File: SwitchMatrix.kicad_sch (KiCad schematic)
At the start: 134 parts, among them K1 Home, K10 I, K11 O, K12 P, K13 Back Space, K14 Delete, K15 1, K16 2, K17 Shift, K18 End, K19 Esc, K2 Tab, K20 A, K21 S, K22 D, K23 F, K24 G, K25 H, K26 J, K27 K, K28 L, K29 ;, K3 Q, K30 ', K31 Return, K32 4, K33 5, K34 Super, K35 Vol +, K36 Shift, K37 Z, K38 X, K39 C, K4 W, K40 V, K41 B, K42 N, K43 M, K44 ,, K45 ., K46 /, K47 Shift, K48 7, K49 8, K5 E, K50 9, K51 N, K52 Vol -, K53 Ctrl, K54 Alt, K55 Super, K56 &dArr;, K57 Blank, K58 &uArr;, K59 Alt, K6 R, K60 0, K61 Enter, K62 Fn, K63 &larr;, K64 &darr;, K7 T, K8 Y, K9 U

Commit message: test prod files for jlc quote, wrong diode footprint 🤦‍
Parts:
- D1, D10, D11, D12, D13, D14, D15, D16, D18, D19, D2, D20, D21, D22, D23, D24, D25, D26, D27, D28, D29, D3, D30, D31, D32, D33, D35, D36, D37, D38, D39, D4, D40, D41, D42, D43, D44, D45, D46, D47, D48, D49, D5, D50, D52, D53, D54, D55, D56, D57, D58, D59, D6, D60, D61, D62, D63, D64, D7, D8, D9: value D -> 1N4148W
- K22: value D -> 1N4148W; footprint PCM_Switch_Keyboard_Hotswap_Kailh:SW_Hotswap_Kailh_MX_1.00u -> Diode_SMD:D_0805_2012Metric_Pad1.15x1.40mm_HandSolder
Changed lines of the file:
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@@
 			)
 		)
-		(property "Value" "D"
+		(property "Value" "1N4148W"
 			(at 39.37 160.02 90)
 			(effects
@@
 			)
 		)
-		(property "Value" "D"
+		(property "Value" "1N4148W"
 			(at 373.38 134.62 90)
 			(effects
@@
 			)
 		)
-		(property "Value" "D"
+		(property "Value" "1N4148W"
 			(at 119.38 139.7 0)
 			(effects
@@
 			)
 		)
-		(property "Footprint" "PCM_Switch_Keyboard_Hotswap_Kailh:SW_Hotswap_Kailh_MX_1.00u"
+		(property "Footprint" "Diode_SMD:D_0805_2012Metric_Pad1.15x1.40mm_HandSolder"
 			(at 119.38 137.16 0)
 			(effects
@@
 			)
 		)
-		(property "Value" "D"
+		(property "Value" "1N4148W"
 			(at 373.38 172.72 90)
 			(effects
@@
 			)
 		)
-		(property "Value" "D"
+		(property "Value" "1N4148W"
 			(at 234.95 172.72 90)
 			(effects
@@
 			)
 		)
-		(property "Value" "D"
+		(property "Value" "1N4148W"
 			(at 105.41 160.02 90)
 			(effects
@@
 			)
 		)
-		(property "Value" "D"
+		(property "Value" "1N4148W"
 			(at 304.8 166.37 90)
 			(effects
@@
 			)
 		)
-		(property "Value" "D"
+		(property "Value" "1N4148W"
 			(at 64.77 160.02 90)
 			(effects
@@
 			)
 		)
-		(property "Value" "D"
+		(property "Value" "1N4148W"
 			(at 105.41 147.32 90)
 			(effects
@@
 			)
 		)
-		(property "Value" "D"
+		(property "Value" "1N4148W"
 			(at 227.33 160.02 90)
 			(effects
@@
 			)
 		)
-		(property "Value" "D"
+		(property "Value" "1N4148W"
 			(at 207.01 160.02 90)
 			(effects
@@
 			)
 		)
-		(property "Value" "D"
+		(property "Value" "1N4148W"
 			(at 353.06 147.32 90)
 			(effects
@@
 			)
 		)
-		(property "Value" "D"
+		(property "Value" "1N4148W"
 			(at 125.73 147.32 90)
 			(effects
@@
 			)
 		)
-		(property "Value" "D"
+		(property "Value" "1N4148W"
 			(at 247.65 134.62 90)
 			(effects
@@
 			)
 		)
-		(property "Value" "D"
+		(property "Value" "1N4148W"
 			(at 64.77 134.62 90)
 			(effects
@@
 			)
 		)
-		(property "Value" "D"
+		(property "Value" "1N4148W"
 			(at 146.05 134.62 90)
 			(effects
@@
 			)
 		)
-		(property "Value" "D"
+		(property "Value" "1N4148W"
 			(at 85.09 147.32 90)
 			(effects
@@
 			)
 		)
-		(property "Value" "D"
+		(property "Value" "1N4148W"
 			(at 207.01 147.32 90)
 			(effects
@@
 			)
 		)
-		(property "Value" "D"
+		(property "Value" "1N4148W"
 			(at 39.37 147.32 90)
 			(effects
@@
 			)
 		)
-		(property "Value" "D"
+		(property "Value" "1N4148W"
 			(at 247.65 147.32 90)
 			(effects
@@
 			)
 		)
-		(property "Value" "D"
+		(property "Value" "1N4148W"
 			(at 125.73 134.62 90)
 			(effects
@@
 			)
 		)
-		(property "Value" "D"
+		(property "Value" "1N4148W"
 			(at 85.09 160.02 90)
 			(effects
@@
 			)
 		)
-		(property "Value" "D"
+		(property "Value" "1N4148W"
 			(at 288.29 134.62 90)
 			(effects
@@
 			)
 		)
-		(property "Value" "D"
+		(property "Value" "1N4148W"
 			(at 67.31 172.72 90)
 			(effects
@@
 			)
 		)
-		(property "Value" "D"
+		(property "Value" "1N4148W"
 			(at 186.69 134.62 90)
 			(effects
@@
 			)
 		)
-		(property "Value" "D"
+		(property "Value" "1N4148W"
 			(at 176.53 172.72 90)
 			(effects
@@
 			)
 		)
-		(property "Value" "D"
+		(property "Value" "1N4148W"
 			(at 118.11 172.72 90)
 			(effects
@@
 			)
 		)
-		(property "Value" "D"
+		(property "Value" "1N4148W"
 			(at 166.37 160.02 90)
 			(effects
@@
 			)
 		)
-		(property "Value" "D"
+		(property "Value" "1N4148W"
 			(at 227.33 147.32 90)
 			(effects
@@
 			)
 		)
-		(property "Value" "D"
+		(property "Value" "1N4148W"
 			(at 92.71 172.72 90)
 			(effects
@@
 			)
 		)
-		(property "Value" "D"
+		(property "Value" "1N4148W"
 			(at 373.38 160.02 90)
 			(effects
@@
 			)
 		)
-		(property "Value" "D"
+		(property "Value" "1N4148W"
 			(at 105.41 134.62 90)
 			(effects
@@
 			)
 		)
-		(property "Value" "D"
+		(property "Value" "1N4148W"
 			(at 353.06 160.02 90)
 			(effects
@@
 			)
 		)
-		(property "Value" "D"
+		(property "Value" "1N4148W"
 			(at 146.05 147.32 90)
 			(effects
@@
 			)
 		)
-		(property "Value" "D"
+		(property "Value" "1N4148W"
 			(at 166.37 134.62 90)
 			(effects
@@
 			)
 		)
-		(property "Value" "D"
+		(property "Value" "1N4148W"
 			(at 209.55 172.72 90)
 			(effects
@@
 			)
 		)
-		(property "Value" "D"
+		(property "Value" "1N4148W"
 			(at 247.65 160.02 90)
 			(effects
@@
 			)
 		)
-		(property "Value" "D"
+		(property "Value" "1N4148W"
 			(at 267.97 147.32 90)
 			(effects
@@
 			)
 		)
-		(property "Value" "D"
+		(property "Value" "1N4148W"
 			(at 331.47 134.62 90)
 			(effects
@@
 			)
 		)
-		(property "Value" "D"
+		(property "Value" "1N4148W"
 			(at 207.01 134.62 90)
 			(effects
@@
 			)
 		)
-		(property "Value" "D"
+		(property "Value" "1N4148W"
 			(at 288.29 147.32 90)
 			(effects
@@
 			)
 		)
-		(property "Value" "D"
+		(property "Value" "1N4148W"
 			(at 39.37 134.62 90)
 			(effects
@@
 			)
 		)
-		(property "Value" "D"
+		(property "Value" "1N4148W"
 			(at 284.48 179.07 90)
 			(effects
@@
 			)
 		)
-		(property "Value" "D"
+		(property "Value" "1N4148W"
 			(at 267.97 134.62 90)
 			(effects
@@
 			)
 		)
-		(property "Value" "D"
+		(property "Value" "1N4148W"
 			(at 304.8 179.07 90)
 			(effects
@@
 			)
 		)
-		(property "Value" "D"
+		(property "Value" "1N4148W"
 			(at 64.77 147.32 90)
 			(effects
@@
 			)
 		)
-		(property "Value" "D"
+		(property "Value" "1N4148W"
 			(at 227.33 134.62 90)
 			(effects
@@
 			)
 		)
-		(property "Value" "D"
+		(property "Value" "1N4148W"
 			(at 353.06 134.62 90)
 			(effects
@@
 			)
 		)
-		(property "Value" "D"
+		(property "Value" "1N4148W"
 			(at 331.47 147.32 90)
 			(effects
@@
 			)
 		)
-		(property "Value" "D"
+		(property "Value" "1N4148W"
 			(at 331.47 160.02 90)
 			(effects
@@
 			)
 		)
-		(property "Value" "D"
+		(property "Value" "1N4148W"
 			(at 39.37 172.72 90)
 			(effects
@@
 			)
 		)
-		(property "Value" "D"
+		(property "Value" "1N4148W"
 			(at 146.05 160.02 90)
 			(effects
@@
 			)
 		)
-		(property "Value" "D"
+		(property "Value" "1N4148W"
 			(at 186.69 160.02 90)
 			(effects
@@
 			)
 		)
-		(property "Value" "D"
+		(property "Value" "1N4148W"
 			(at 373.38 147.32 90)
 			(effects
@@
 			)
 		)
-		(property "Value" "D"
+		(property "Value" "1N4148W"
 			(at 125.73 160.02 90)
 			(effects
@@
 			)
 		)
-		(property "Value" "D"
+		(property "Value" "1N4148W"
 			(at 267.97 160.02 90)
 			(effects
@@
 			)
 		)
-		(property "Value" "D"
+		(property "Value" "1N4148W"
 			(at 353.06 172.72 90)
 			(effects
@@
 			)
 		)
-		(property "Value" "D"
+		(property "Value" "1N4148W"
 			(at 143.51 172.72 90)
 			(effects
@@
 			)
 		)
-		(property "Value" "D"
+		(property "Value" "1N4148W"
 			(at 85.09 134.62 90)
 			(effects
@@
 			)
 		)
-		(property "Value" "D"
+		(property "Value" "1N4148W"
 			(at 186.69 147.32 90)
 			(effects
@@
 			)
 		)
-		(property "Value" "D"
+		(property "Value" "1N4148W"
 			(at 166.37 147.32 90)
 			(effects
@@
 			)
 		)
-		(property "Value" "D"
+		(property "Value" "1N4148W"
 			(at 325.12 179.07 90)
 			(effects

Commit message: sod-128 diodes, still wrong it was supposed to be 123
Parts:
- D1, D10, D11, D12, D13, D14, D15, D16, D18, D19, D2, D20, D21, D22, D23, D24, D25, D26, D27, D28, D29, D3, D30, D31, D32, D33, D35, D36, D37, D38, D39, D4, D40, D41, D42, D43, D44, D45, D46, D47, D48, D49, D5, D50, D52, D53, D54, D55, D56, D57, D58, D59, D6, D60, D61, D62, D63, D64, D7, D8, D9: footprint Diode_SMD:D_0805_2012Metric_Pad1.15x1.40mm_HandSolder -> Diode_SMD:D_SOD-123
- K22: footprint Diode_SMD:D_0805_2012Metric_Pad1.15x1.40mm_HandSolder -> PCM_Switch_Keyboard_Hotswap_Kailh:SW_Hotswap_Kailh_MX_1.00u

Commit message: last before prod
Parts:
- K22: value 1N4148W -> D
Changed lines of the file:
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@@
 			)
 		)
-		(property "Value" "1N4148W"
+		(property "Value" "D"
 			(at 119.38 139.7 0)
 			(effects

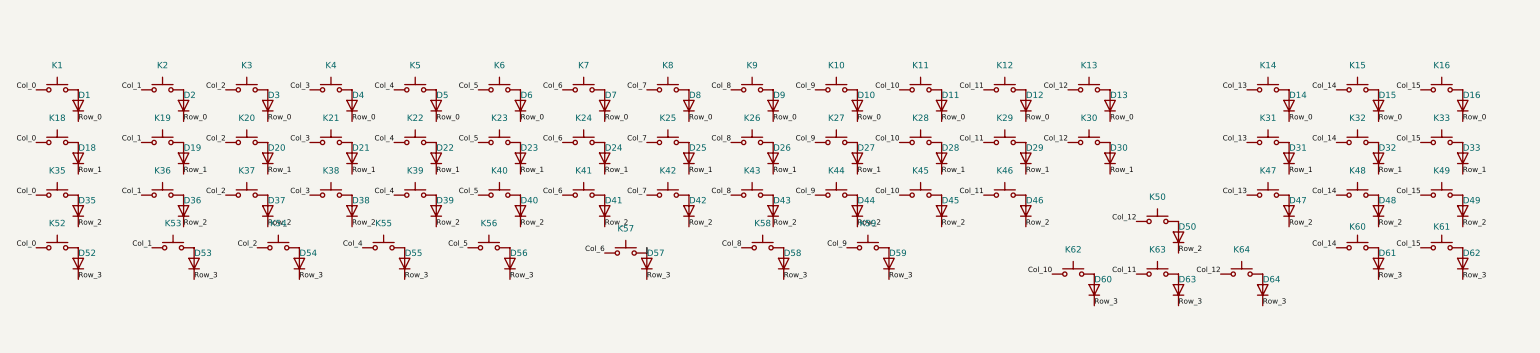
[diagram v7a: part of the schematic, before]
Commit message: add part nums for bom
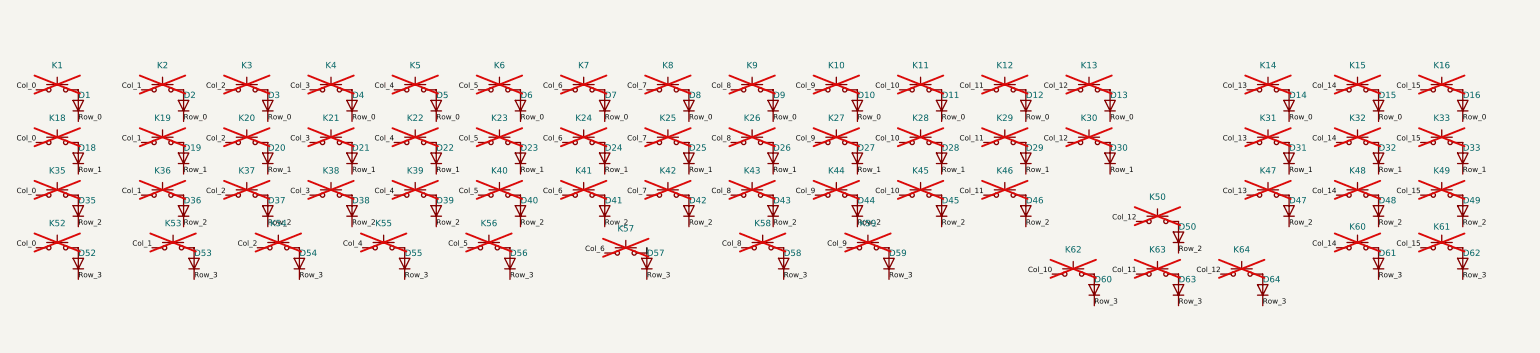
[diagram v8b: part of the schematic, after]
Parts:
- D1, D10, D11, D12, D13, D14, D15, D16, D18, D19, D2, D20, D21, D22, D23, D24, D25, D26, D27, D28, D29, D3, D30, D31, D32, D33, D35, D36, D37, D38, D39, D4, D40, D41, D42, D43, D44, D45, D46, D47, D48, D49, D5, D50, D52, D53, D54, D55, D56, D57, D58, D59, D6, D60, D61, D62, D63, D64, D7, D8, D9: LCSC (none) -> C2828417; Manufacturer (none) -> 1N4148W; Type (none) -> SMD
- D17, D34, D51: Type (none) -> DNS
- JP10, JP2, JP3, JP4, JP5, JP9: now left out of the parts list
- K1: value Home -> Kailh Hotswap Socket; Comment (none) -> Do Not Substitute; Digikey (none) -> 1528-4958-ND; MPN (none) -> 4958; Manufacturer (none) -> Adafruit; Type (none) -> SMD; now not fitted
- K10: value I -> Kailh Hotswap Socket; Comment (none) -> Do Not Substitute; Digikey (none) -> 1528-4958-ND; MPN (none) -> 4958; Manufacturer (none) -> Adafruit; Type (none) -> SMD; now not fitted
- K11: value O -> Kailh Hotswap Socket; Comment (none) -> Do Not Substitute; Digikey (none) -> 1528-4958-ND; MPN (none) -> 4958; Manufacturer (none) -> Adafruit; Type (none) -> SMD; now not fitted
- K12: value P -> Kailh Hotswap Socket; Comment (none) -> Do Not Substitute; Digikey (none) -> 1528-4958-ND; MPN (none) -> 4958; Manufacturer (none) -> Adafruit; Type (none) -> SMD; now not fitted
- K13: value Back Space -> Kailh Hotswap Socket; Comment (none) -> Do Not Substitute; Digikey (none) -> 1528-4958-ND; MPN (none) -> 4958; Manufacturer (none) -> Adafruit; Type (none) -> SMD; now not fitted
- K14: value Delete -> Kailh Hotswap Socket; Comment (none) -> Do Not Substitute; Digikey (none) -> 1528-4958-ND; MPN (none) -> 4958; Manufacturer (none) -> Adafruit; Type (none) -> SMD; now not fitted
- K15: value 1 -> Kailh Hotswap Socket; Comment (none) -> Do Not Substitute; Digikey (none) -> 1528-4958-ND; MPN (none) -> 4958; Manufacturer (none) -> Adafruit; Type (none) -> SMD; now not fitted
- K16: value 2 -> Kailh Hotswap Socket; Comment (none) -> Do Not Substitute; Digikey (none) -> 1528-4958-ND; MPN (none) -> 4958; Manufacturer (none) -> Adafruit; Type (none) -> SMD; now not fitted
- K17: value Shift -> Kailh Hotswap Socket; Comment (none) -> Do Not Substitute; Digikey (none) -> 1528-4958-ND; MPN (none) -> 4958; Manufacturer (none) -> Adafruit; Type (none) -> SMD
- K18: value End -> Kailh Hotswap Socket; Comment (none) -> Do Not Substitute; Digikey (none) -> 1528-4958-ND; MPN (none) -> 4958; Manufacturer (none) -> Adafruit; Type (none) -> SMD; now not fitted
- K19: value Esc -> Kailh Hotswap Socket; Comment (none) -> Do Not Substitute; Digikey (none) -> 1528-4958-ND; MPN (none) -> 4958; Manufacturer (none) -> Adafruit; Type (none) -> SMD; now not fitted
- K2: value Tab -> Kailh Hotswap Socket; Comment (none) -> Do Not Substitute; Digikey (none) -> 1528-4958-ND; MPN (none) -> 4958; Manufacturer (none) -> Adafruit; Type (none) -> SMD; now not fitted
- K20: value A -> Kailh Hotswap Socket; Comment (none) -> Do Not Substitute; Digikey (none) -> 1528-4958-ND; MPN (none) -> 4958; Manufacturer (none) -> Adafruit; Type (none) -> SMD; now not fitted
- K21: value S -> Kailh Hotswap Socket; Comment (none) -> Do Not Substitute; Digikey (none) -> 1528-4958-ND; MPN (none) -> 4958; Manufacturer (none) -> Adafruit; Type (none) -> SMD; now not fitted
- K22: value D -> Kailh Hotswap Socket; Comment (none) -> Do Not Substitute; Digikey (none) -> 1528-4958-ND; MPN (none) -> 4958; Manufacturer (none) -> Adafruit; Type (none) -> SMD; now not fitted
- K23: value F -> Kailh Hotswap Socket; Comment (none) -> Do Not Substitute; Digikey (none) -> 1528-4958-ND; MPN (none) -> 4958; Manufacturer (none) -> Adafruit; Type (none) -> SMD; now not fitted
- K24: value G -> Kailh Hotswap Socket; Comment (none) -> Do Not Substitute; Digikey (none) -> 1528-4958-ND; MPN (none) -> 4958; Manufacturer (none) -> Adafruit; Type (none) -> SMD; now not fitted
- K25: value H -> Kailh Hotswap Socket; Comment (none) -> Do Not Substitute; Digikey (none) -> 1528-4958-ND; MPN (none) -> 4958; Manufacturer (none) -> Adafruit; Type (none) -> SMD; now not fitted
- K26: value J -> Kailh Hotswap Socket; Comment (none) -> Do Not Substitute; Digikey (none) -> 1528-4958-ND; MPN (none) -> 4958; Manufacturer (none) -> Adafruit; Type (none) -> SMD; now not fitted
- K27: value K -> Kailh Hotswap Socket; Comment (none) -> Do Not Substitute; Digikey (none) -> 1528-4958-ND; MPN (none) -> 4958; Manufacturer (none) -> Adafruit; Type (none) -> SMD; now not fitted
- K28: value L -> Kailh Hotswap Socket; Comment (none) -> Do Not Substitute; Digikey (none) -> 1528-4958-ND; MPN (none) -> 4958; Manufacturer (none) -> Adafruit; Type (none) -> SMD; now not fitted
- K29: value ; -> Kailh Hotswap Socket; Comment (none) -> Do Not Substitute; Digikey (none) -> 1528-4958-ND; MPN (none) -> 4958; Manufacturer (none) -> Adafruit; Type (none) -> SMD; now not fitted
- K3: value Q -> Kailh Hotswap Socket; Comment (none) -> Do Not Substitute; Digikey (none) -> 1528-4958-ND; MPN (none) -> 4958; Manufacturer (none) -> Adafruit; Type (none) -> SMD; now not fitted
- K30: value ' -> Kailh Hotswap Socket; Comment (none) -> Do Not Substitute; Digikey (none) -> 1528-4958-ND; MPN (none) -> 4958; Manufacturer (none) -> Adafruit; Type (none) -> SMD; now not fitted
- K31: value Return -> Kailh Hotswap Socket; Comment (none) -> Do Not Substitute; Digikey (none) -> 1528-4958-ND; MPN (none) -> 4958; Manufacturer (none) -> Adafruit; Type (none) -> SMD; now not fitted
- K32: value 4 -> Kailh Hotswap Socket; Comment (none) -> Do Not Substitute; Digikey (none) -> 1528-4958-ND; MPN (none) -> 4958; Manufacturer (none) -> Adafruit; Type (none) -> SMD; now not fitted
- K33: value 5 -> Kailh Hotswap Socket; Comment (none) -> Do Not Substitute; Digikey (none) -> 1528-4958-ND; MPN (none) -> 4958; Manufacturer (none) -> Adafruit; Type (none) -> SMD; now not fitted
- K34: value Super -> Kailh Hotswap Socket; Comment (none) -> Do Not Substitute; Digikey (none) -> 1528-4958-ND; MPN (none) -> 4958; Manufacturer (none) -> Adafruit; Type (none) -> SMD
- K35: value Vol + -> Kailh Hotswap Socket; Comment (none) -> Do Not Substitute; Digikey (none) -> 1528-4958-ND; MPN (none) -> 4958; Manufacturer (none) -> Adafruit; Type (none) -> SMD; now not fitted
- K36, K47: value Shift -> Kailh Hotswap Socket; Comment (none) -> Do Not Substitute; Digikey (none) -> 1528-4958-ND; MPN (none) -> 4958; Manufacturer (none) -> Adafruit; Type (none) -> SMD; now not fitted
- K37: value Z -> Kailh Hotswap Socket; Comment (none) -> Do Not Substitute; Digikey (none) -> 1528-4958-ND; MPN (none) -> 4958; Manufacturer (none) -> Adafruit; Type (none) -> SMD; now not fitted
- K38: value X -> Kailh Hotswap Socket; Comment (none) -> Do Not Substitute; Digikey (none) -> 1528-4958-ND; MPN (none) -> 4958; Manufacturer (none) -> Adafruit; Type (none) -> SMD; now not fitted
- K39: value C -> Kailh Hotswap Socket; Comment (none) -> Do Not Substitute; Digikey (none) -> 1528-4958-ND; MPN (none) -> 4958; Manufacturer (none) -> Adafruit; Type (none) -> SMD; now not fitted
- K4: value W -> Kailh Hotswap Socket; Comment (none) -> Do Not Substitute; Digikey (none) -> 1528-4958-ND; MPN (none) -> 4958; Manufacturer (none) -> Adafruit; Type (none) -> SMD; now not fitted
- K40: value V -> Kailh Hotswap Socket; Comment (none) -> Do Not Substitute; Digikey (none) -> 1528-4958-ND; MPN (none) -> 4958; Manufacturer (none) -> Adafruit; Type (none) -> SMD; now not fitted
- K41: value B -> Kailh Hotswap Socket; Comment (none) -> Do Not Substitute; Digikey (none) -> 1528-4958-ND; MPN (none) -> 4958; Manufacturer (none) -> Adafruit; Type (none) -> SMD; now not fitted
- K42: value N -> Kailh Hotswap Socket; Comment (none) -> Do Not Substitute; Digikey (none) -> 1528-4958-ND; MPN (none) -> 4958; Manufacturer (none) -> Adafruit; Type (none) -> SMD; now not fitted
- K43: value M -> Kailh Hotswap Socket; Comment (none) -> Do Not Substitute; Digikey (none) -> 1528-4958-ND; MPN (none) -> 4958; Manufacturer (none) -> Adafruit; Type (none) -> SMD; now not fitted
- K44: value , -> Kailh Hotswap Socket; Comment (none) -> Do Not Substitute; Digikey (none) -> 1528-4958-ND; MPN (none) -> 4958; Manufacturer (none) -> Adafruit; Type (none) -> SMD; now not fitted
- K45: value . -> Kailh Hotswap Socket; Comment (none) -> Do Not Substitute; Digikey (none) -> 1528-4958-ND; MPN (none) -> 4958; Manufacturer (none) -> Adafruit; Type (none) -> SMD; now not fitted
- K46: value / -> Kailh Hotswap Socket; Comment (none) -> Do Not Substitute; Digikey (none) -> 1528-4958-ND; MPN (none) -> 4958; Manufacturer (none) -> Adafruit; Type (none) -> SMD; now not fitted
- K48: value 7 -> Kailh Hotswap Socket; Comment (none) -> Do Not Substitute; Digikey (none) -> 1528-4958-ND; MPN (none) -> 4958; Manufacturer (none) -> Adafruit; Type (none) -> SMD; now not fitted
- K49: value 8 -> Kailh Hotswap Socket; Comment (none) -> Do Not Substitute; Digikey (none) -> 1528-4958-ND; MPN (none) -> 4958; Manufacturer (none) -> Adafruit; Type (none) -> SMD; now not fitted
- K5: value E -> Kailh Hotswap Socket; Comment (none) -> Do Not Substitute; Digikey (none) -> 1528-4958-ND; MPN (none) -> 4958; Manufacturer (none) -> Adafruit; Type (none) -> SMD; now not fitted
- K50: value 9 -> Kailh Hotswap Socket; Comment (none) -> Do Not Substitute; Digikey (none) -> 1528-4958-ND; MPN (none) -> 4958; Manufacturer (none) -> Adafruit; Type (none) -> SMD; now not fitted
- K51: value N -> Kailh Hotswap Socket; Comment (none) -> Do Not Substitute; Digikey (none) -> 1528-4958-ND; MPN (none) -> 4958; Manufacturer (none) -> Adafruit; Type (none) -> SMD
- K52: value Vol - -> Kailh Hotswap Socket; Comment (none) -> Do Not Substitute; Digikey (none) -> 1528-4958-ND; MPN (none) -> 4958; Manufacturer (none) -> Adafruit; Type (none) -> SMD; now not fitted
- K53: value Ctrl -> Kailh Hotswap Socket; Comment (none) -> Do Not Substitute; Digikey (none) -> 1528-4958-ND; MPN (none) -> 4958; Manufacturer (none) -> Adafruit; Type (none) -> SMD; now not fitted
- K54, K59: value Alt -> Kailh Hotswap Socket; Comment (none) -> Do Not Substitute; Digikey (none) -> 1528-4958-ND; MPN (none) -> 4958; Manufacturer (none) -> Adafruit; Type (none) -> SMD; now not fitted
- K55: value Super -> Kailh Hotswap Socket; Comment (none) -> Do Not Substitute; Digikey (none) -> 1528-4958-ND; MPN (none) -> 4958; Manufacturer (none) -> Adafruit; Type (none) -> SMD; now not fitted
- K56: value &dArr; -> Kailh Hotswap Socket; Comment (none) -> Do Not Substitute; Digikey (none) -> 1528-4958-ND; MPN (none) -> 4958; Manufacturer (none) -> Adafruit; Type (none) -> SMD; now not fitted
- K57: value Blank -> Kailh Hotswap Socket; Comment (none) -> Do Not Substitute; Digikey (none) -> 1528-4958-ND; MPN (none) -> 4958; Manufacturer (none) -> Adafruit; Type (none) -> SMD; now not fitted
- K58: value &uArr; -> Kailh Hotswap Socket; Comment (none) -> Do Not Substitute; Digikey (none) -> 1528-4958-ND; MPN (none) -> 4958; Manufacturer (none) -> Adafruit; Type (none) -> SMD; now not fitted
- K6: value R -> Kailh Hotswap Socket; Comment (none) -> Do Not Substitute; Digikey (none) -> 1528-4958-ND; MPN (none) -> 4958; Manufacturer (none) -> Adafruit; Type (none) -> SMD; now not fitted
- K60: value 0 -> Kailh Hotswap Socket; Comment (none) -> Do Not Substitute; Digikey (none) -> 1528-4958-ND; MPN (none) -> 4958; Manufacturer (none) -> Adafruit; Type (none) -> SMD; now not fitted
- K61: value Enter -> Kailh Hotswap Socket; Comment (none) -> Do Not Substitute; Digikey (none) -> 1528-4958-ND; MPN (none) -> 4958; Manufacturer (none) -> Adafruit; Type (none) -> SMD; now not fitted
- K62: value Fn -> Kailh Hotswap Socket; Comment (none) -> Do Not Substitute; Digikey (none) -> 1528-4958-ND; MPN (none) -> 4958; Manufacturer (none) -> Adafruit; Type (none) -> SMD; now not fitted
- K63: value &larr; -> Kailh Hotswap Socket; Comment (none) -> Do Not Substitute; Digikey (none) -> 1528-4958-ND; MPN (none) -> 4958; Manufacturer (none) -> Adafruit; Type (none) -> SMD; now not fitted
- K64: value &darr; -> Kailh Hotswap Socket; Comment (none) -> Do Not Substitute; Digikey (none) -> 1528-4958-ND; MPN (none) -> 4958; Manufacturer (none) -> Adafruit; Type (none) -> SMD; now not fitted
- K7: value T -> Kailh Hotswap Socket; Comment (none) -> Do Not Substitute; Digikey (none) -> 1528-4958-ND; MPN (none) -> 4958; Manufacturer (none) -> Adafruit; Type (none) -> SMD; now not fitted
- K8: value Y -> Kailh Hotswap Socket; Comment (none) -> Do Not Substitute; Digikey (none) -> 1528-4958-ND; MPN (none) -> 4958; Manufacturer (none) -> Adafruit; Type (none) -> SMD; now not fitted
- K9: value U -> Kailh Hotswap Socket; Comment (none) -> Do Not Substitute; Digikey (none) -> 1528-4958-ND; MPN (none) -> 4958; Manufacturer (none) -> Adafruit; Type (none) -> SMD; now not fitted
